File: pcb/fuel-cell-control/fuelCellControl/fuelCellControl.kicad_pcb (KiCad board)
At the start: 2 copper layers, 40 parts, among them J1 Conn_01x02_Male, J2 Conn_01x15_Male, J3 LittlePump, J4 BigPump, J5 Conn_01x15_Male, J6 Relay, J7 Conn_01x10_Male, J8 Conn_01x10_Male, Q1 Q_NMOS_GDS, Q2 Q_NMOS_GDS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

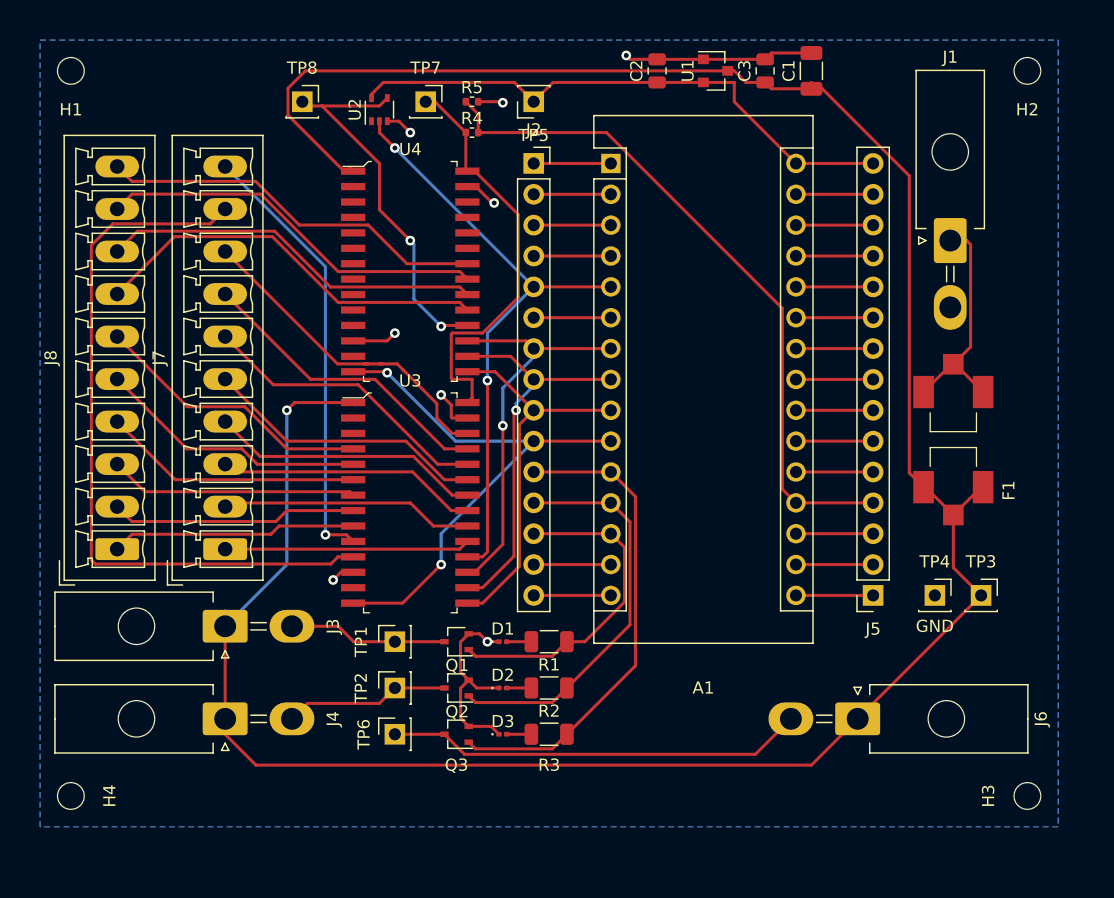
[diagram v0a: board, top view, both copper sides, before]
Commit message: enlarged power traces
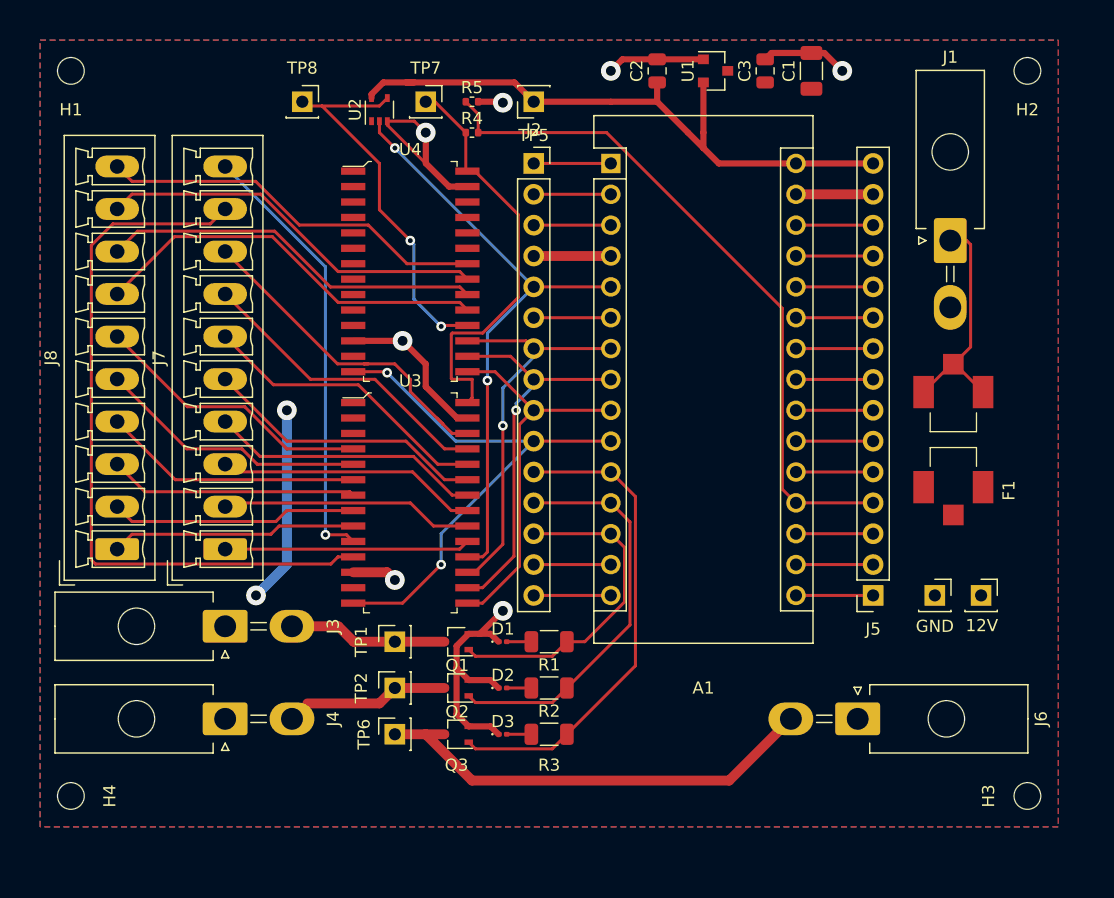
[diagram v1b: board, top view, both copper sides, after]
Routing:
- net +12V: track 211.5 -> 16.6 mm, vias 1 -> 2
- net GND: track 62.4 -> 82.6 mm, vias 8 -> 7
- net +5V: track 48.6 -> 53.3 mm
- net Net-(J6-Pad2): track 34.5 -> 37.8 mm
- added copper zone on F.Cu, net +12V
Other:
- net class Power added: clearance 0.2, trace_width 0.8128, via_dia 0.8, via_drill 0.4
- board text added: "12V"

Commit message: updated based on design review
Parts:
- removed U2: 74AHCT1G04, Package_TO_SOT_SMD:SOT-353_SC-70-5
- added C4: 0.1uF, Capacitor_SMD:C_0603_1608Metric, F.Cu at (91.4, 95.2)
- added R6: 820k, Resistor_SMD:R_0603_1608Metric, F.Cu at (101.6, 71.1)
- added R7: 430k, Resistor_SMD:R_0603_1608Metric, F.Cu at (101.6, 68.6)
- C1: value 10uF -> 1uF; footprint Capacitor_SMD:C_1206_3216Metric -> Capacitor_SMD:C_0603_1608Metric
- C2: value 0.1uF -> 1uF; footprint Capacitor_SMD:C_0805_2012Metric -> Capacitor_SMD:C_0603_1608Metric
- C3: footprint Capacitor_SMD:C_0805_2012Metric -> Capacitor_SMD:C_0603_1608Metric
- D1, D2, D3: footprint LED_SMD:LED_0201_0603Metric -> LED_SMD:LED_0603_1608Metric
- H1, H2, H3, H4: footprint MountingHole:MountingHole_2.2mm_M2 -> MountingHole:MountingHole_3.2mm_M3
- J1: value Conn_01x02_Male -> InputPower
- Q1, Q2, Q3: footprint Package_TO_SOT_SMD:SOT-323_SC-70 -> Package_TO_SOT_SMD:SOT-89-3
- R1, R2, R3: value 400ohms -> 1.5k; footprint Resistor_SMD:R_1206_3216Metric -> Resistor_SMD:R_0603_1608Metric
- R4: value 680k -> 820k; footprint Resistor_SMD:R_0402_1005Metric -> Resistor_SMD:R_0603_1608Metric
- R5: value 470k -> 430k; footprint Resistor_SMD:R_0402_1005Metric -> Resistor_SMD:R_0603_1608Metric
- TP1: value TestPoint -> LPump
- TP2: value TestPoint -> BPump
- TP3: value TestPoint -> 12V
- TP4: value TestPoint -> GND
- TP5: value TestPoint -> 5V
- TP6: value TestPoint -> RelayT
- TP7: value TestPoint -> Mux1
- TP8: value TestPoint -> Mux2
- moved C3 37.9 mm to (91.4, 74.9)
- moved TP6 30.5 mm to (128.3, 119.4)
- moved TP5 28.1 mm to (137.2, 66.0)
- moved Q3 19.4 mm to (121.9, 124.5), turned to 0 degrees
- moved TP8 15.3 mm to (105.4, 67.3)
- moved H4 12.7 mm to (71.1, 113.0)
- moved R3 12.7 mm to (123.2, 120.7)
- moved D3 12.7 mm to (119.4, 120.7)
- moved TP2 11.7 mm to (95.2, 128.3)
- moved Q2 11.5 mm to (101.6, 128.3)
- moved J4 8.98 mm to (82.5, 128.3)
- moved J3 8.98 mm to (82.5, 120.7)
- moved TP7 8.98 mm to (91.4, 67.3)
- moved TP1 8.03 mm to (95.2, 120.7)
- moved Q1 7.73 mm to (101.6, 120.7)
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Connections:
- A1 pad 27: /Nano5VOut -> +5V
- A1 pad 30: +5V -> /VinNano
- A1 pad 5: /EnablePin -> /D2
- J2 pad 5: /EnablePin -> /D2
- J5 pad 12: /Nano5VOut -> +5V
- J5 pad 15: +5V -> /VinNano
- TP8 pad 1: Net-(TP8-Pad1) -> Net-(R6-Pad1)
- U3 pad 18: /EnablePin -> +12V
- U4 pad 18: Net-(TP8-Pad1) -> +12V
- U4 pad 28: Net-(R4-Pad1) -> Net-(R6-Pad1)
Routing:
- net /Analog1: track 6.35 -> 60.3 mm
- net /EnablePin: track 50.5 -> 0.00 mm, vias 2 -> 0
- net Net-(TP8-Pad1): track 31.8 -> 0.00 mm, vias 2 -> 0
- net Net-(J6-Pad2): track 37.8 -> 18.3 mm
- net /BigPump: track 33.2 -> 45.1 mm
- net /MuxAnalog: track 56.8 -> 68.5 mm
- net +5V: track 53.3 -> 42.6 mm
- net Net-(R6-Pad1): track 0.00 -> 10.6 mm, vias 0 -> 2
- net /LittlePump: track 27.3 -> 36.7 mm
- net GND: track 82.6 -> 76.1 mm, vias 7 -> 11
- net /VinNano: track 0.00 -> 6.35 mm
- net /Nano5VOut: track 6.35 -> 0.00 mm
- net /D2: track 0.00 -> 6.35 mm
- net Net-(F1-Pad2): track 19.0 -> 23.2 mm
- net /Relay: track 39.9 -> 36.1 mm
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
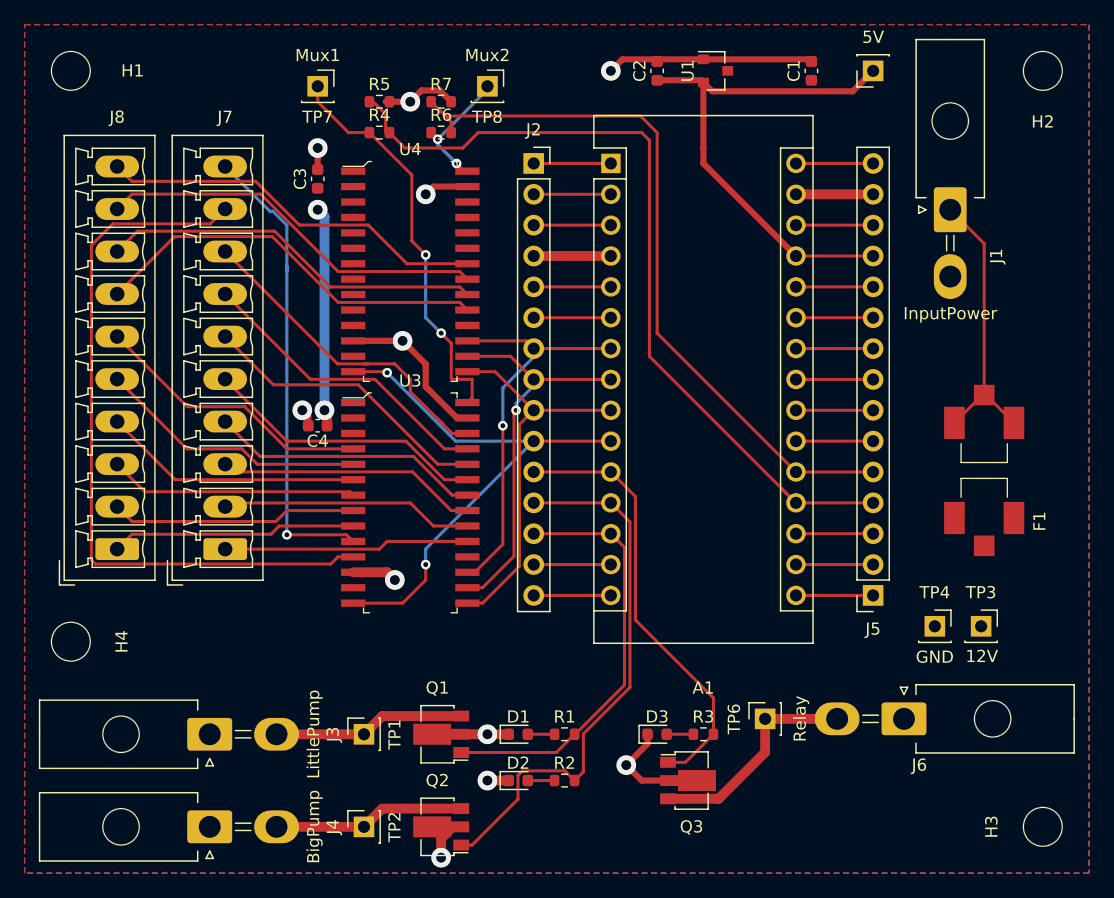
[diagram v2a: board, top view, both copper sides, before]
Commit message: cleans up some longer traces
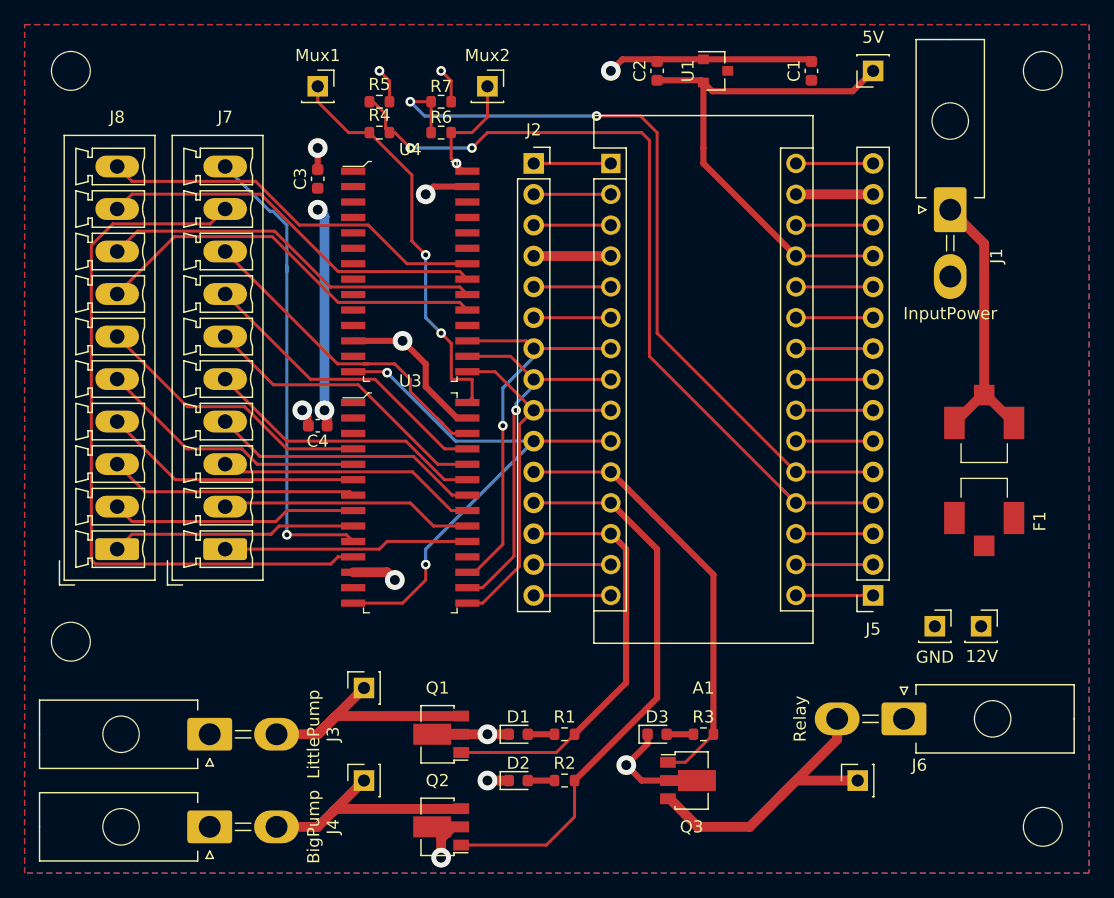
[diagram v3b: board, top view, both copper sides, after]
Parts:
- moved TP6 9.16 mm to (135.9, 124.5)
- moved TP2 3.81 mm to (95.2, 124.5)
- moved TP1 3.81 mm to (95.2, 116.8)
- turned R6 to 180 degrees
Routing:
- net Net-(J6-Pad2): track 18.3 -> 26.4 mm
- net Net-(J3-Pad2): track 15.8 -> 21.2 mm
- net /Analog1: track 60.3 -> 64.7 mm, vias 0 -> 2
- net Net-(J4-Pad2): track 15.8 -> 19.4 mm
- net /BigPump: track 45.1 -> 46.9 mm
- net /LittlePump: track 36.7 -> 35.1 mm
- net Net-(R6-Pad1): track 10.6 -> 10.2 mm, vias 2 -> 1
- net GND: track 76.1 -> 75.8 mm, vias 11 -> 12
- net /MuxAnalog: track 68.5 -> 68.6 mm, vias 0 -> 2

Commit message: remove voltage regulator and update connector spacing and tracing
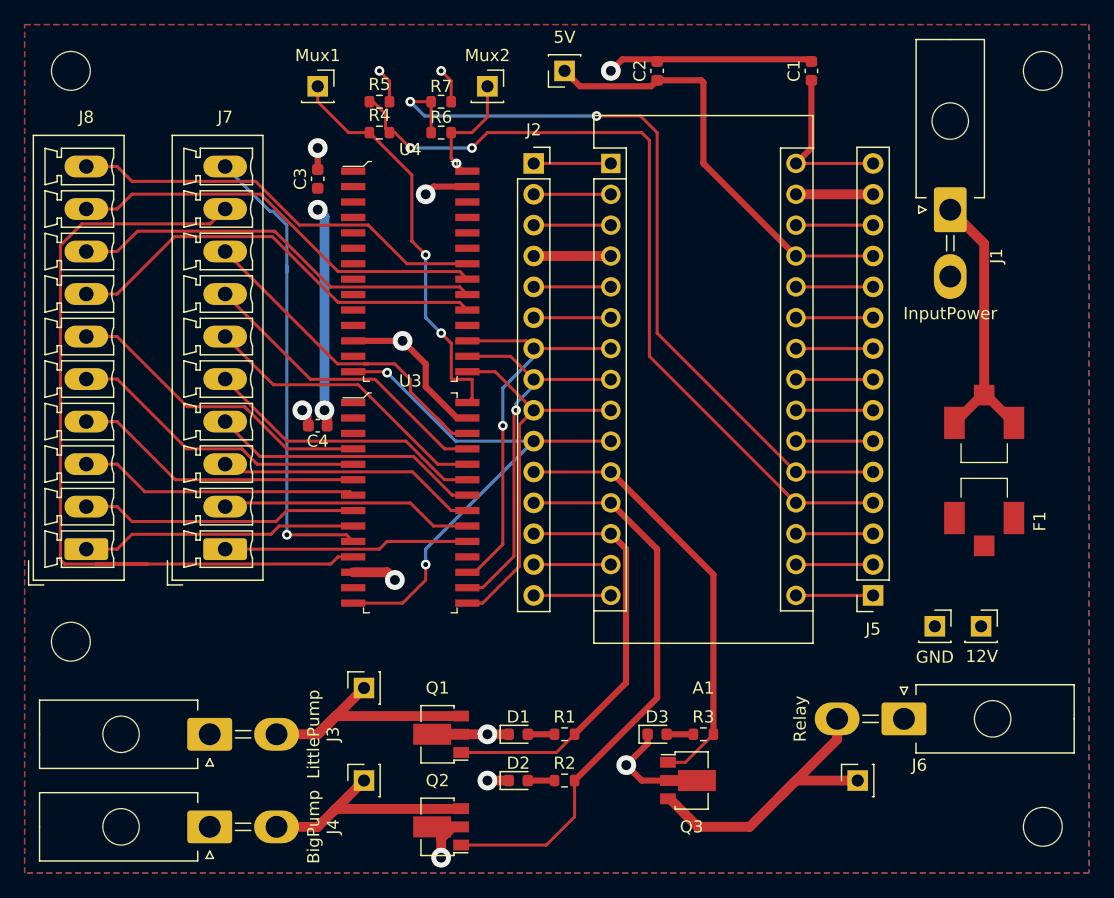
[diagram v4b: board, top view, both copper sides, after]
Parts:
- removed U1: MCP1754S-3302xCB, Package_TO_SOT_SMD:SOT-23
- moved TP5 25.4 mm to (111.8, 66.0)
- moved J8 2.54 mm to (72.4, 105.4)
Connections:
- A1 pad 30: /VinNano -> +12V
- J5 pad 15: /VinNano -> +12V
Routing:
- net +12V: track 18.4 -> 32.1 mm
- net Net-(J7-Pad9): track 60.1 -> 69.5 mm
- net +5V: track 42.6 -> 36.0 mm
- net /VinNano: track 6.35 -> 0.00 mm
- net Net-(J8-Pad9): track 32.2 -> 34.8 mm
- net Net-(J8-Pad7): track 33.3 -> 35.8 mm
- net Net-(J8-Pad6): track 24.0 -> 26.5 mm
- net Net-(J8-Pad5): track 23.0 -> 25.5 mm
- net Net-(J8-Pad4): track 21.4 -> 24.0 mm
- net Net-(J8-Pad3): track 20.5 -> 23.0 mm
- net Net-(J8-Pad2): track 20.3 -> 22.9 mm
- net Net-(J8-Pad10): track 32.1 -> 34.7 mm
- net Net-(J8-Pad1): track 20.2 -> 22.8 mm
- net Net-(J8-Pad8): track 31.7 -> 34.2 mm

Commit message: adds supermileage logo and updates part information
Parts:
- added G***: LOGO, digikey-footprints:supermileagelogo3, B.Cu at (111.8, 118.1)
- J2, J5: value Conn_01x15_Male -> Conn_01x15_Female
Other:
- board text added: "Fuel Cell Control v1.0 by Michelle Li"

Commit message: rev1.0 schematic
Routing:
- net Net-(F1-Pad2): track 23.2 -> 0.32 mm
- added copper zone on F.Cu, net Net-(F1-Pad2)
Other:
- board outline added: 87.6 x 69.9 mm

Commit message: track day updates
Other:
- net class Default removed
- net class Power removed
